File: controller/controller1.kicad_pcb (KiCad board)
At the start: 2 copper layers, 153 x 113 mm, 56 parts, among them J2 Female XLR Out, J3 Male XLR In, J4 SJ-3523-SMT

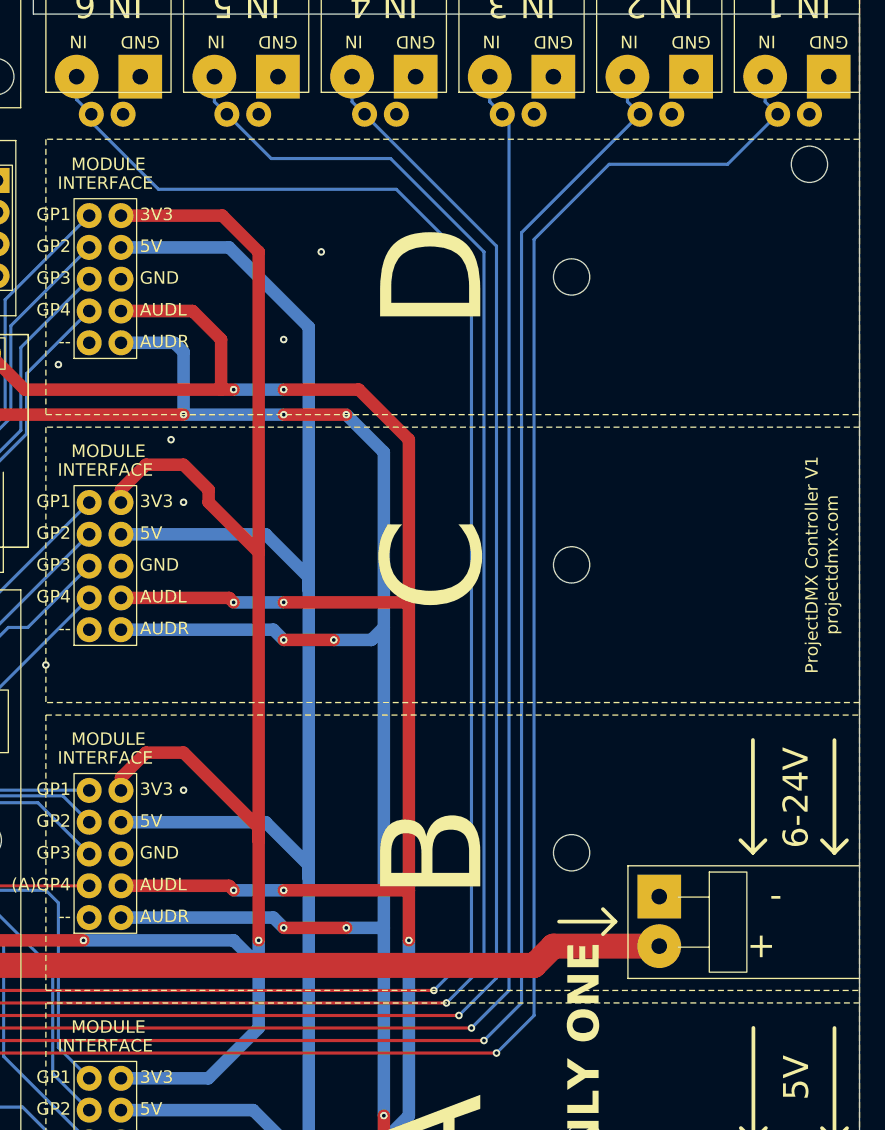
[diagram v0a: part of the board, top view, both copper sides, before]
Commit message: move input jst alt pins closer to overlap term pins
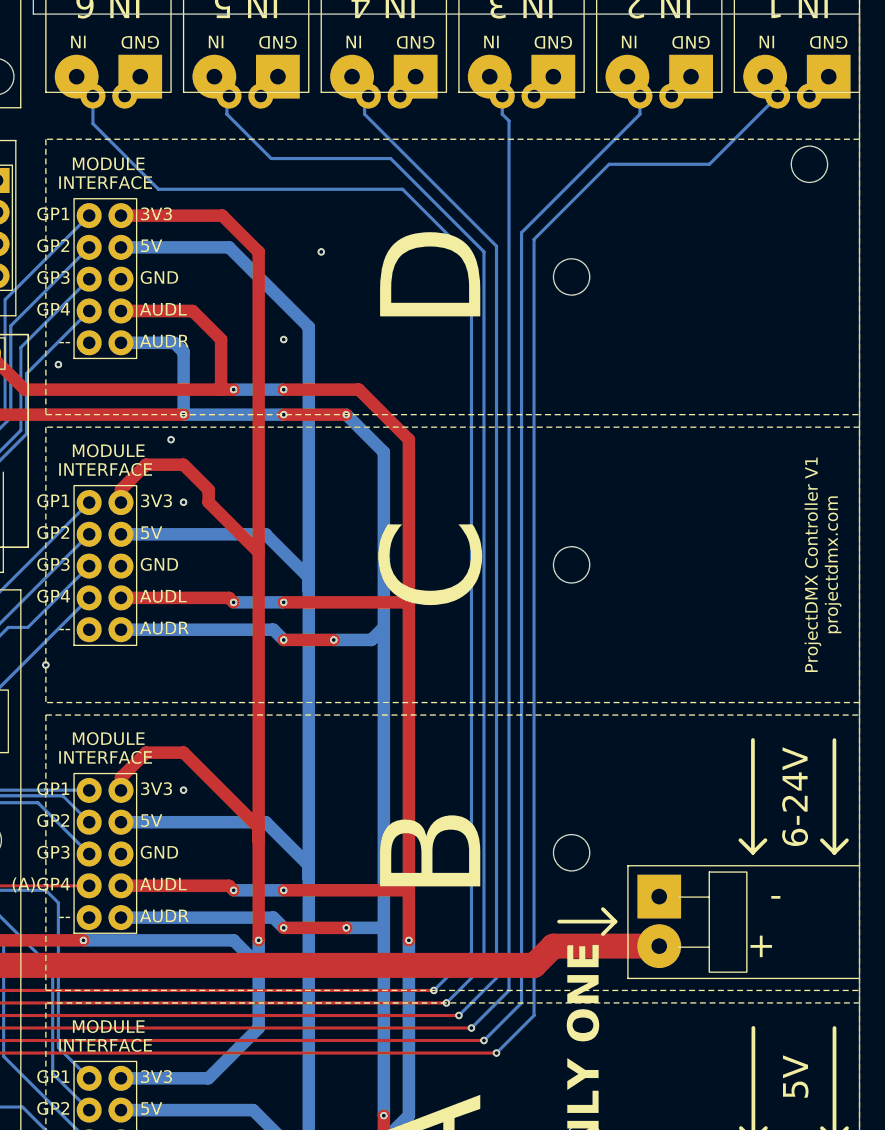
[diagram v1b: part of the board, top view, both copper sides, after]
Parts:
- moved ? 1.48 mm to (206.3, 53.5)
- moved ? 1.48 mm to (203.8, 53.5)
- moved ? 1.46 mm to (195.2, 53.5)
- moved ? 1.46 mm to (192.6, 53.5)
- moved ? 1.46 mm to (184.3, 53.5)
- moved ? 1.46 mm to (181.8, 53.5)
- moved ? 1.45 mm to (225.5, 53.5)
- moved ? 1.45 mm to (228.0, 53.5)
- moved ? 1.45 mm to (214.5, 53.5)
- moved ? 1.45 mm to (217.0, 53.5)
- moved ? 1.45 mm to (236.5, 53.5)
- moved ? 1.45 mm to (239.0, 53.5)
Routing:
- net Net-(U1-AGP42): track 194.5 -> 191.7 mm
- net Net-(U1-AGP44): track 172.1 -> 170.2 mm
- net Net-(U1-AGP43): track 184.3 -> 182.4 mm
- net Net-(U1-AGP45): track 172.2 -> 170.3 mm
- net Net-(U1-AGP46): track 170.6 -> 168.7 mm
- net Net-(U1-AGP47): track 173.6 -> 171.8 mm

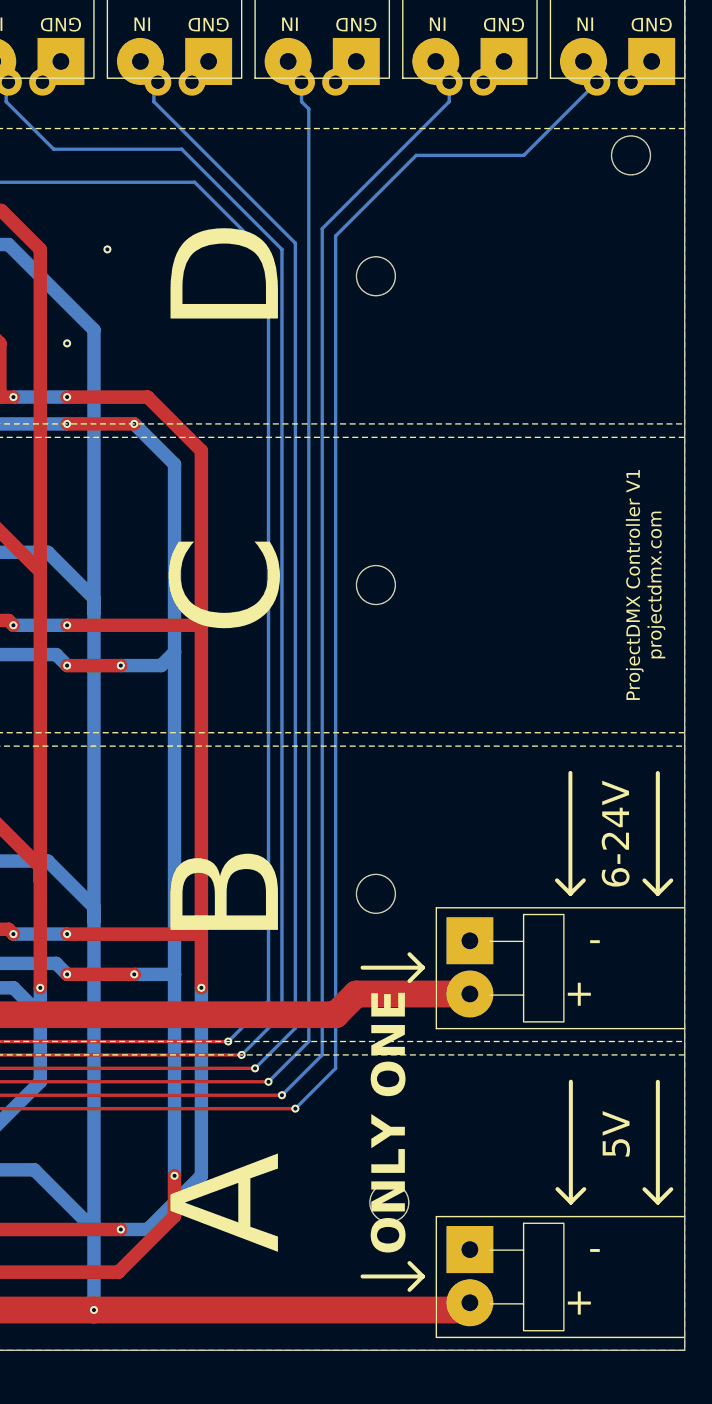
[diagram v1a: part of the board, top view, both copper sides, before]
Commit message: move mounting holes on modules and controller
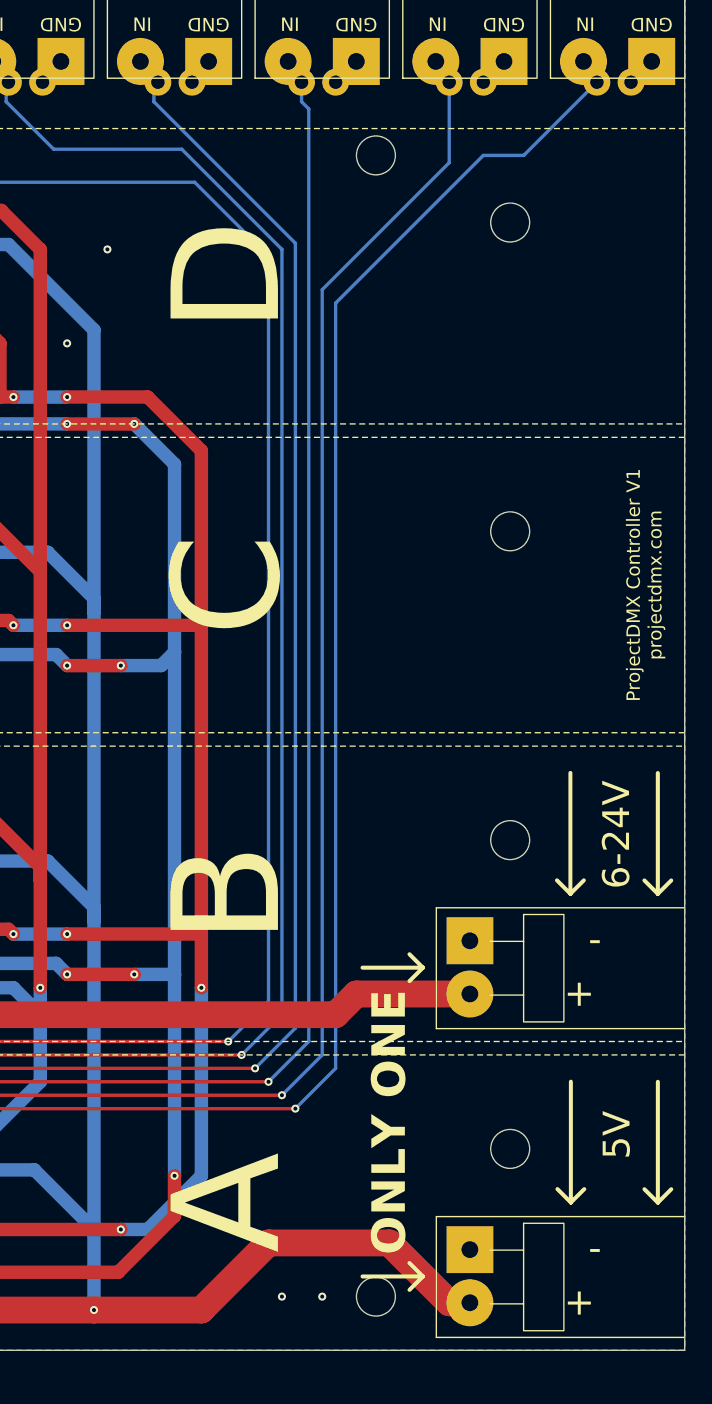
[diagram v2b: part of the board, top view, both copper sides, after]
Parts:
- removed the REF** at (220.0, 68.0)
- removed the REF** at (220.0, 91.0)
- removed the REF** at (221.0, 137.0)
- removed the REF** at (220.0, 114.0)
- added ?: , , F.Cu at (220.0, 144.0)
- added ?: , , F.Cu at (230.0, 133.0)
- added ?: , , F.Cu at (230.0, 64.0)
- added ?: , , F.Cu at (230.0, 110.0)
- added ?: , , F.Cu at (230.0, 87.0)
- moved ? 19.0 mm to (220.0, 59.0)
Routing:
- net 5V: track 412.9 -> 417.4 mm
- net Net-(U1-AGP42): track 191.7 -> 188.7 mm
- net GND: vias 22 -> 24

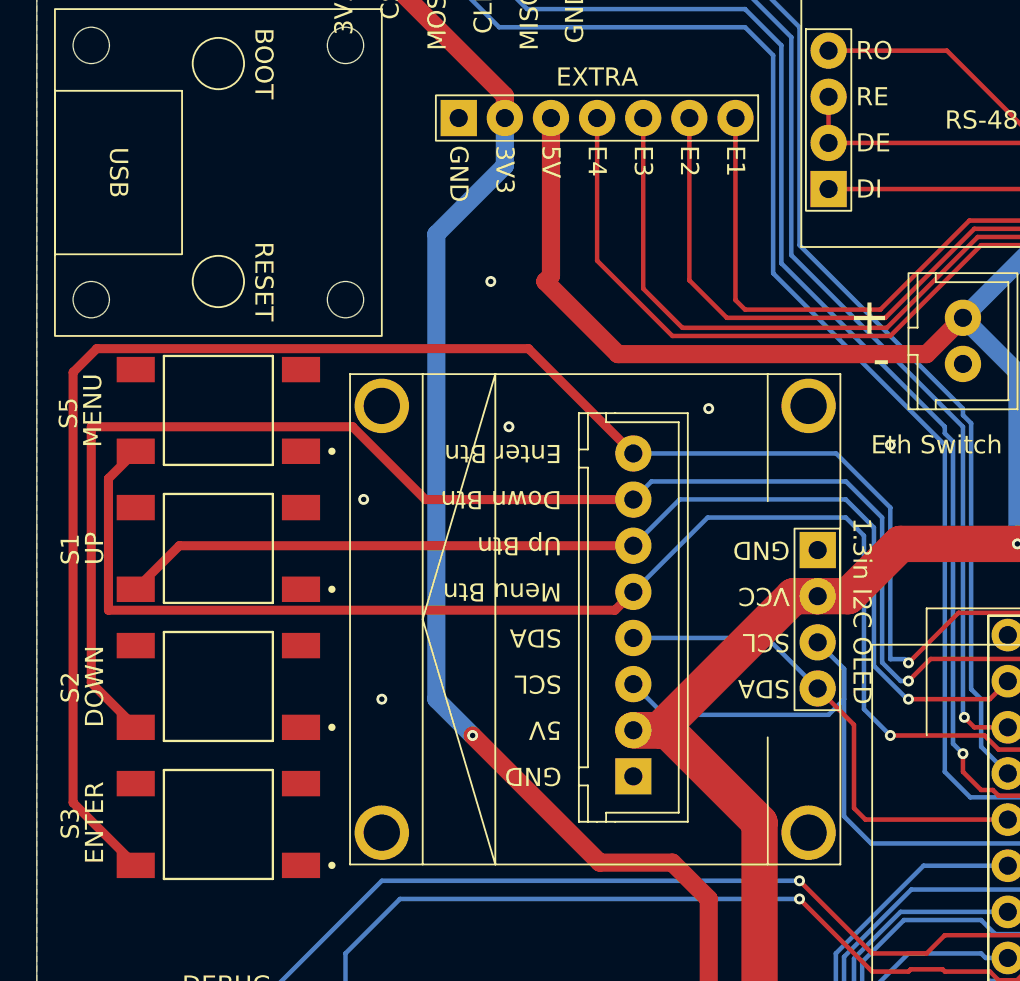
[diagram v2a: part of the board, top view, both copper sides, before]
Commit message: adjust footprints and cleanup stuff
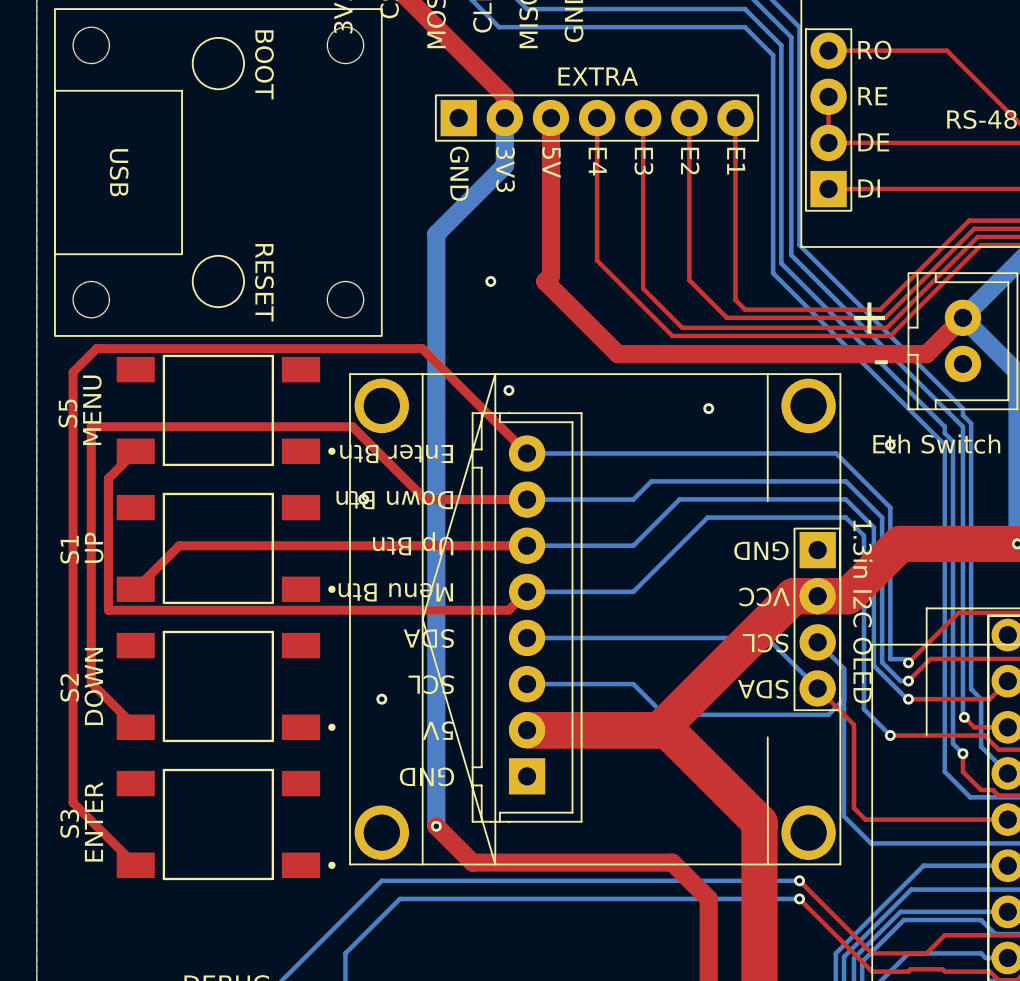
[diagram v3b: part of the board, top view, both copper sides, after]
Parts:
- moved U26 5.85 mm to (117.0, 100.2)
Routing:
- net 5V: track 417.4 -> 429.1 mm
- net Net-(U1-GP39): track 37.2 -> 43.1 mm
- net Net-(U1-GP38): track 27.5 -> 33.3 mm
- net 3V3: track 294.9 -> 299.0 mm

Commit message: finish everything
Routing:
- net GND: vias 24 -> 50
- net (no net): vias 0 -> 1
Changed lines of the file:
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@@
 			(drillshape 0)
 			(scaleselection 1)
-			(outputdirectory "E:/Downloads/mian1/")
+			(outputdirectory "E:/Projects/ProjectDMX/controller/")
 		)
 	)
@@
 		)
 	)
+	(via
+		(at 75 86)
+		(size 0.6)
+		(drill 0.3)
+		(layers "F.Cu" "B.Cu")
+		(net 0)
+	)
 	(segment
 		(start 160.589 54.981)
@@
 	)
 	(via
+		(at 135.5 70)
+		(size 0.6)
+		(drill 0.3)
+		(layers "F.Cu" "B.Cu")
+		(free yes)
+		(net 2)
+	)
+	(via
 		(at 116 79)
 		(size 0.6)
@@
 	)
 	(via
+		(at 115 41.5)
+		(size 0.6)
+		(drill 0.3)
+		(layers "F.Cu" "B.Cu")
+		(free yes)
+		(net 2)
+	)
+	(via
 		(at 168 79)
 		(size 0.6)
@@
 	)
 	(via
+		(at 161.5 81.5)
+		(size 0.6)
+		(drill 0.3)
+		(layers "F.Cu" "B.Cu")
+		(free yes)
+		(net 2)
+	)
+	(via
 		(at 197 73)
 		(size 0.6)
@@
 	)
 	(via
+		(at 145 59)
+		(size 0.6)
+		(drill 0.3)
+		(layers "F.Cu" "B.Cu")
+		(free yes)
+		(net 2)
+	)
+	(via
 		(at 140 136)
 		(size 0.6)
@@
 	)
 	(via
+		(at 99.5 42)
+		(size 0.6)
+		(drill 0.3)
+		(layers "F.Cu" "B.Cu")
+		(free yes)
+		(net 2)
+	)
+	(via
 		(at 200 66)
 		(size 0.6)
@@
 	)
 	(via
+		(at 141.5 37.5)
+		(size 0.6)
+		(drill 0.3)
+		(layers "F.Cu" "B.Cu")
+		(free yes)
+		(net 2)
+	)
+	(via
+		(at 173 86)
+		(size 0.6)
+		(drill 0.3)
+		(layers "F.Cu" "B.Cu")
+		(free yes)
+		(net 2)
+	)
+	(via
 		(at 189 86)
 		(size 0.6)
@@
 	)
 	(via
+		(at 221.5 98)
+		(size 0.6)
+		(drill 0.3)
+		(layers "F.Cu" "B.Cu")
+		(free yes)
+		(net 2)
+	)
+	(via
+		(at 122 132)
+		(size 0.6)
+		(drill 0.3)
+		(layers "F.Cu" "B.Cu")
+		(free yes)
+		(net 2)
+	)
+	(via
 		(at 216 144)
 		(size 0.6)
@@
 	)
 	(via
+		(at 100 95)
+		(size 0.6)
+		(drill 0.3)
+		(layers "F.Cu" "B.Cu")
+		(free yes)
+		(net 2)
+	)
+	(via
+		(at 99 50)
+		(size 0.6)
+		(drill 0.3)
+		(layers "F.Cu" "B.Cu")
+		(free yes)
+		(net 2)
+	)
+	(via
 		(at 213 144)
 		(size 0.6)
@@
 	)
 	(via
+		(at 174 105)
+		(size 0.6)
+		(drill 0.3)
+		(layers "F.Cu" "B.Cu")
+		(free yes)
+		(net 2)
+	)
+	(via
 		(at 105 140)
 		(size 0.6)
@@
 	)
 	(via
+		(at 125 90.5)
+		(size 0.6)
+		(drill 0.3)
+		(layers "F.Cu" "B.Cu")
+		(free yes)
+		(net 2)
+	)
+	(via
+		(at 208 75)
+		(size 0.6)
+		(drill 0.3)
+		(layers "F.Cu" "B.Cu")
+		(free yes)
+		(net 2)
+	)
+	(via
+		(at 189 99.5)
+		(size 0.6)
+		(drill 0.3)
+		(layers "F.Cu" "B.Cu")
+		(free yes)
+		(net 2)
+	)
+	(via
 		(at 188 81)
 		(size 0.6)
@@
 	)
 	(via
+		(at 171.5 41.5)
+		(size 0.6)
+		(drill 0.3)
+		(layers "F.Cu" "B.Cu")
+		(free yes)
+		(net 2)
+	)
+	(via
 		(at 155 51)
 		(size 0.6)
@@
 	)
 	(via
+		(at 100 84.5)
+		(size 0.6)
+		(drill 0.3)
+		(layers "F.Cu" "B.Cu")
+		(free yes)
+		(net 2)
+	)
+	(via
 		(at 115 73)
 		(size 0.6)
@@
 	)
 	(via
+		(at 210 98)
+		(size 0.6)
+		(drill 0.3)
+		(layers "F.Cu" "B.Cu")
+		(free yes)
+		(net 2)
+	)
+	(via
+		(at 95 130.5)
+		(size 0.6)
+		(drill 0.3)
+		(layers "F.Cu" "B.Cu")
+		(free yes)
+		(net 2)
+	)
+	(via
 		(at 122 123)
 		(size 0.6)
@@
 	)
 	(via
+		(at 122 101)
+		(size 0.6)
+		(drill 0.3)
+		(layers "F.Cu" "B.Cu")
+		(free yes)
+		(net 2)
+	)
+	(via
 		(at 171 138)
 		(size 0.6)
@@
 	)
 	(via
+		(at 120 112)
+		(size 0.6)
+		(drill 0.3)
+		(layers "F.Cu" "B.Cu")
+		(free yes)
+		(net 2)
+	)
+	(via
+		(at 204.5 63.5)
+		(size 0.6)
+		(drill 0.3)
+		(layers "F.Cu" "B.Cu")
+		(free yes)
+		(net 2)
+	)
+	(via
 		(at 127 80)
 		(size 0.6)
@@
 	)
 	(via
+		(at 95 108.5)
+		(size 0.6)
+		(drill 0.3)
+		(layers "F.Cu" "B.Cu")
+		(free yes)
+		(net 2)
+	)
+	(via
+		(at 220.5 86.5)
+		(size 0.6)
+		(drill 0.3)
+		(layers "F.Cu" "B.Cu")
+		(free yes)
+		(net 2)
+	)
+	(via
+		(at 219.5 73.5)
+		(size 0.6)
+		(drill 0.3)
+		(layers "F.Cu" "B.Cu")
+		(free yes)
+		(net 2)
+	)
+	(via
 		(at 179 75)
 		(size 0.6)
 		(drill 0.3)
+		(layers "F.Cu" "B.Cu")
+		(free yes)
+		(net 2)
+	)
+	(via
+		(at 103 66.5)
+		(size 0.6)
+		(drill 0.3)

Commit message: small changes
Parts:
- moved REF** 9.41 mm to (233.9, 115.1)
- moved REF** 9.35 mm to (233.8, 138.0)
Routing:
- net 5V: track 429.1 -> 439.3 mm
- net VCC: track 66.7 -> 76.1 mm
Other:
- board size 153 x 113 mm -> 160 x 113 mm
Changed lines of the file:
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@@
 		)
 		(pad "" np_thru_hole circle
-			(at 0 0)
+			(at 15 0)
 			(size 2.9 2.9)
 			(drill 2.9)
@@
 		)
 		(pad "" np_thru_hole circle
-			(at 0 0)
+			(at 15 0)
 			(size 2.9 2.9)
 			(drill 2.9)
@@
 	(footprint "ProjectDMX:JST VH"
 		(layer "F.Cu")
-		(at 224.5 115.04)
+		(at 233.913589 115.061449)
 		(property "Reference" "REF**"
 			(at 0 -0.5 0)
@@
 			(remove_unused_layers no)
 			(net 2 "GND")
+			(zone_connect 2)
 		)
 		(pad "2" thru_hole circle
@@
 		)
 		(pad "" np_thru_hole circle
-			(at 0 0)
+			(at 15 0)
 			(size 2.9 2.9)
 			(drill 2.9)
@@
 	(footprint "ProjectDMX:JST VH"
 		(layer "F.Cu")
-		(at 224.5 138.04)
+		(at 233.85 138.04)
 		(property "Reference" "REF**"
 			(at 0 -0.5 0)
@@
 			(remove_unused_layers no)
 			(net 2 "GND")
+			(zone_connect 2)
 		)
 		(pad "2" thru_hole circle
@@
 		)
 		(pad "" np_thru_hole circle
-			(at 0 0)
+			(at 15 0)
 			(size 2.9 2.9)
 			(drill 2.9)
@@
 	(gr_line
 		(start 178 103)
-		(end 243 103)
+		(end 250 103)
 		(stroke
 			(width 0.05)
@@
 	)
 	(gr_line
-		(start 243 126)
+		(start 250 126)
 		(end 178 126)
 		(stroke
@@
 	)
 	(gr_line
-		(start 243 57)
+		(start 250 57)
 		(end 178 57)
 		(stroke
@@
 	(gr_line
 		(start 178 79)
-		(end 243 79)
+		(end 250 79)
 		(stroke
 			(width 0.05)
@@
 	)
 	(gr_line
-		(start 243 102)
+		(start 250 102)
 		(end 178 102)
 		(stroke
@@
 	)
 	(gr_line
-		(start 243 80)
+		(start 250 80)
 		(end 178 80)
 		(stroke
@@
 	(gr_line
 		(start 178 125)
-		(end 243 125)
+		(end 250 125)
 		(stroke
 			(width 0.05)
@@
 	)
 	(gr_line
-		(start 243 47)
-		(end 243 148)
+		(start 250 47)
+		(end 250 148)
 		(stroke
 			(width 0.05)
@@
 	)
 	(gr_line
-		(start 243 47)
+		(start 250 47)
 		(end 177 47)
 		(stroke
@@
 	)
 	(gr_line
-		(start 243 148)
+		(start 250 148)
 		(end 90 148)
 		(stroke
@@
 	)
 	(segment
-		(start 212 140)
-		(end 207 145)
-		(width 2)
-		(layer "F.Cu")
-		(net 7)
-	)
-	(segment
-		(start 227 144.46)
-		(end 225.46 144.46)
+		(start 129.799 118.799)
+		(end 129.799 102.797)
 		(width 2)
 		(layer "F.Cu")
@@
 	)
 	(segment
-		(start 129.799 118.799)
-		(end 129.799 102.797)
+		(start 214 138)
+		(end 207 145)
 		(width 2)
 		(layer "F.Cu")
@@
 	)
 	(segment
+		(start 236.35 144.46)
+		(end 231.46 144.46)
+		(width 2)
+		(layer "F.Cu")
+		(net 7)
+	)
+	(segment
 		(start 133 90.33)
 		(end 134.67 90.33)
@@
 	)
 	(segment
-		(start 221 140)
-		(end 212 140)
+		(start 231.46 144.46)
+		(end 225 138)
+		(width 2)
+		(layer "F.Cu")
+		(net 7)
+	)
+	(segment
+		(start 225 138)
+		(end 214 138)
 		(width 2)
 		(layer "F.Cu")
@@
 	)
 	(segment
+		(start 207 145)
+		(end 199 145)
+		(width 2)
+		(layer "F.Cu")
+		(net 7)
+	)
+	(segment
 		(start 139 77)
 		(end 141 75)
@@
 	)
 	(segment
-		(start 227 144.46)
-		(end 226.46 145)
-		(width 2)
-		(layer "F.Cu")
-		(net 7)
-	)
-	(segment
 		(start 124.29 97.71)
 		(end 131.67 90.33)
@@
 		(net 7)
 	)
-	(segment
-		(start 225.46 144.46)
-		(end 221 140)
-		(width 2)
-		(layer "F.Cu")
-		(net 7)
-	)
-	(segment
-		(start 207 145)
-		(end 199 145)
-		(width 2)
-		(layer "F.Cu")
-		(net 7)
-	)
 	(via
 		(at 173 142)
@@
 	)
 	(segment
-		(start 227 121.46)
+		(start 236.39214 121.46)
 		(end 218.54 121.46)
 		(width 2)
@@
 	)
 	(segment
-		(start 171.133593 125)
-		(end 171 125)
+		(start 171 125)
+		(end 164.5 131.5)
 		(width 2)
 		(layer "F.Cu")
@@
 	)
 	(segment
-		(start 171 125)
-		(end 164.5 131.5)
+		(start 236.413589 121.481449)
+		(end 236.39214 121.46)
+		(width 2)
+		(layer "F.Cu")
+		(net 8)
+	)
+	(segment
+		(start 171.133593 125)
+		(end 171 125)
 		(width 2)
 		(layer "F.Cu")
@@
 		(polygon
 			(pts
-				(xy 90 35) (xy 243 35) (xy 243 148) (xy 90 148)
+				(xy 90 35) (xy 250 35) (xy 250 148) (xy 90 148)
 			)
 		)
